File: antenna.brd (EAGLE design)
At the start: 95 x 95 mm, 21 parts, among them X1 BU-SMA-V

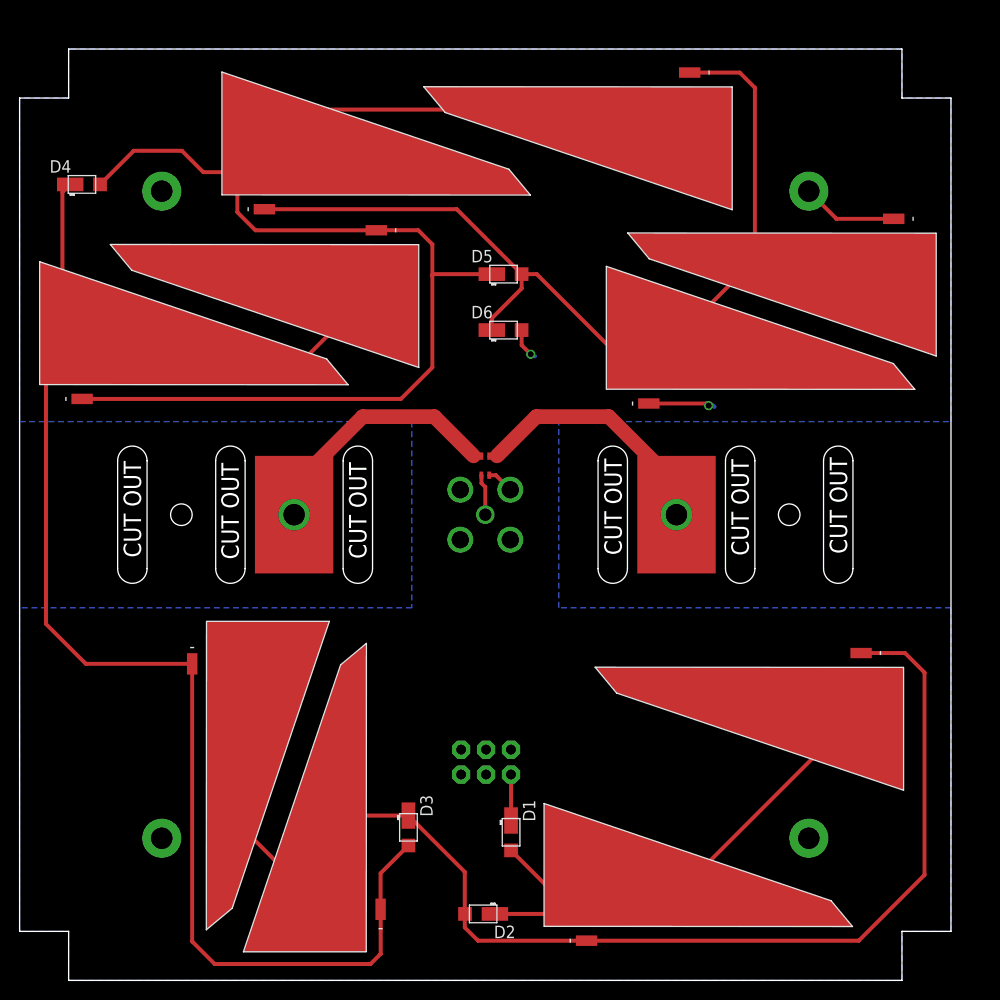
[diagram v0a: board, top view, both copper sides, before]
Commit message: Updates to antenna board
Fixed corner cutout dimensions. Added 3-pin Molex connector. Added
“CUTOUT” text to dimension layer.
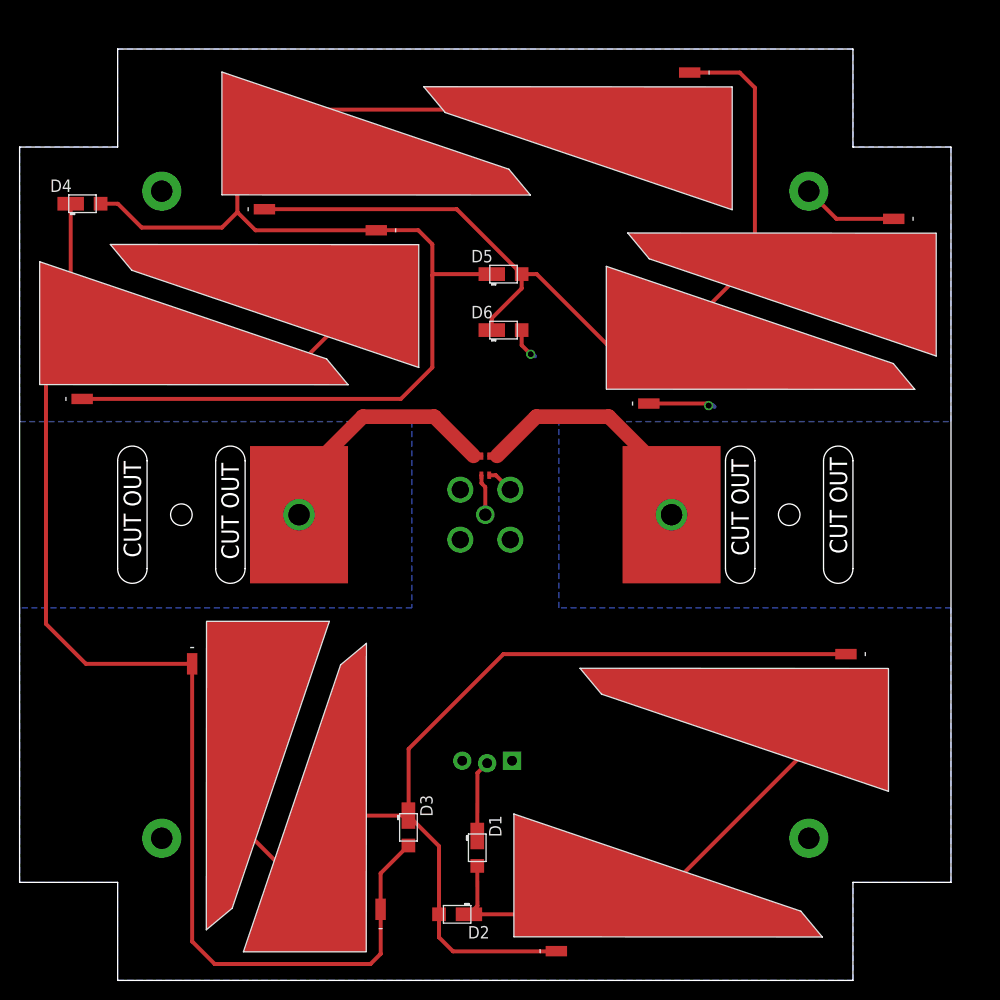
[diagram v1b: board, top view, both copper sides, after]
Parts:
- JP1: device SparkFun-Connectors:2X3 -> SparkFun-Connectors:MOLEX-1X3_LOCK
- moved D1 3.79 mm to (46.7, 13.5)
- moved SL1 3.26 mm to (57.8, 4.57)
- moved D2 2.65 mm to (44.6, 6.74)
- moved D4 1.97 mm to (6.41, 79.2)
- moved SL2 1.54 mm to (81.3, 31.7)
- moved JP1 1.28 mm to (50.2, 22.3)
- moved U$1 0.50 mm to (28.5, 47.5)
- moved U$2 0.50 mm to (66.5, 47.5)
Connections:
- net GND: now also JP1.1; no longer JP1.2
- net V_SOLAR: now also JP1.2; no longer JP1.1
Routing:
- net N$45: track 140.8 -> 130.7 mm
- net V_SOLAR: track 4.69 -> 7.83 mm
- net N$37: track 161.6 -> 160.2 mm
- net N$9: track 56.8 -> 57.7 mm
- net N$39: track 148.2 -> 147.6 mm
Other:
- outline, holes or cut-outs redrawn

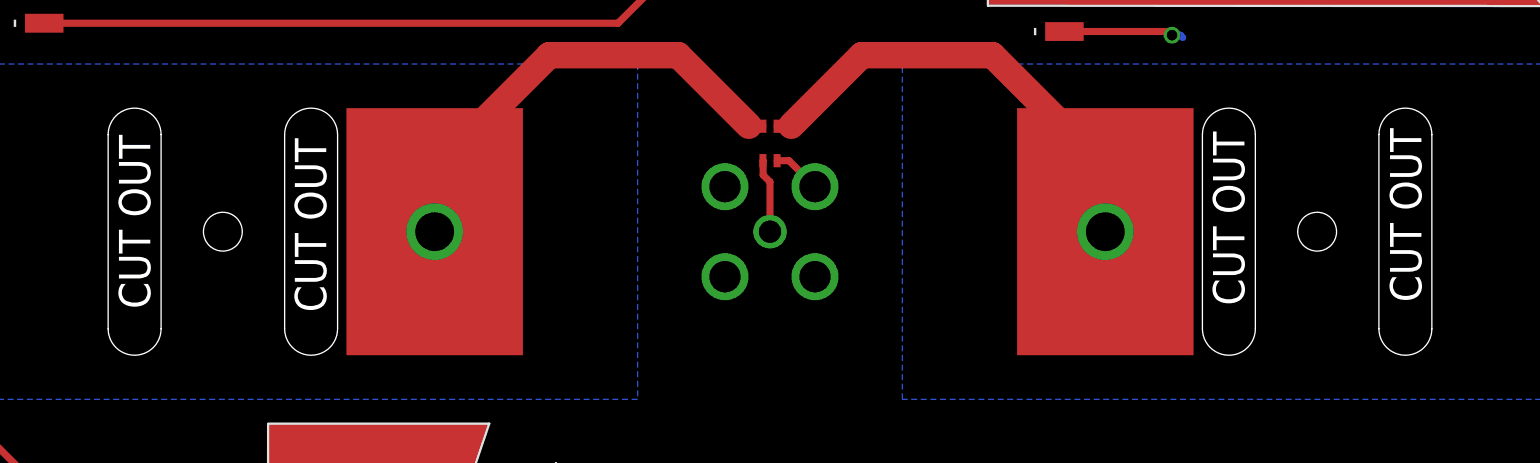
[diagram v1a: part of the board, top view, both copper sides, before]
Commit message: Increased cutout line width
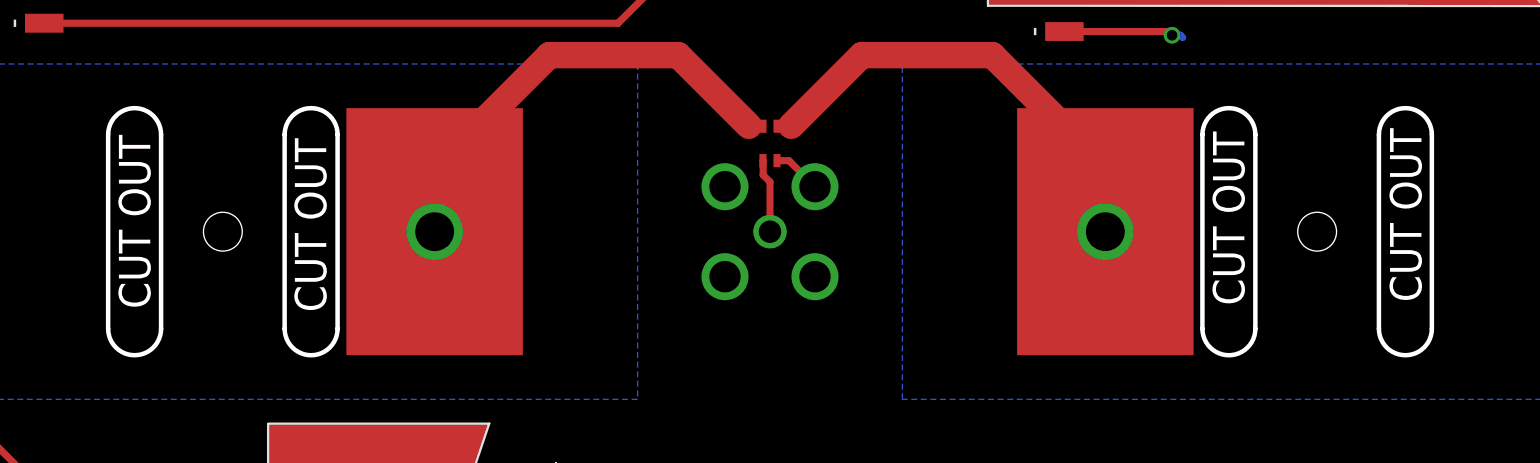
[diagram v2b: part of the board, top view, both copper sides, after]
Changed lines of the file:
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@@
 <wire x1="10" y1="85" x2="0" y2="85" width="0" layer="20"/>
 <wire x1="0" y1="85" x2="0" y2="10" width="0" layer="20"/>
-<wire x1="75" y1="53" x2="75" y2="42" width="0" layer="20"/>
-<wire x1="72" y1="42" x2="72" y2="53" width="0" layer="20"/>
-<wire x1="10" y1="42" x2="10" y2="53" width="0" layer="20"/>
-<wire x1="13" y1="53" x2="13" y2="42" width="0" layer="20"/>
-<wire x1="20" y1="42" x2="20" y2="53" width="0" layer="20"/>
-<wire x1="23" y1="53" x2="23" y2="42" width="0" layer="20"/>
-<wire x1="10" y1="53" x2="13" y2="53" width="0" layer="20" curve="-180" cap="flat"/>
-<wire x1="13" y1="42" x2="10" y2="42" width="0" layer="20" curve="-180" cap="flat"/>
-<wire x1="20" y1="53" x2="23" y2="53" width="0" layer="20" curve="-180" cap="flat"/>
-<wire x1="23" y1="42" x2="20" y2="42" width="0" layer="20" curve="-180" cap="flat"/>
-<wire x1="72" y1="53" x2="75" y2="53" width="0" layer="20" curve="-180" cap="flat"/>
-<wire x1="75" y1="42" x2="72" y2="42" width="0" layer="20" curve="-180" cap="flat"/>
-<wire x1="85" y1="53" x2="85" y2="42" width="0" layer="20"/>
-<wire x1="82" y1="42" x2="82" y2="53" width="0" layer="20"/>
-<wire x1="82" y1="53" x2="85" y2="53" width="0" layer="20" curve="-180" cap="flat"/>
-<wire x1="85" y1="42" x2="82" y2="42" width="0" layer="20" curve="-180" cap="flat"/>
+<wire x1="75" y1="53" x2="75" y2="42" width="0.254" layer="20"/>
+<wire x1="72" y1="42" x2="72" y2="53" width="0.254" layer="20"/>
+<wire x1="10" y1="42" x2="10" y2="53" width="0.254" layer="20"/>
+<wire x1="13" y1="53" x2="13" y2="42" width="0.254" layer="20"/>
+<wire x1="20" y1="42" x2="20" y2="53" width="0.254" layer="20"/>
+<wire x1="23" y1="53" x2="23" y2="42" width="0.254" layer="20"/>
+<wire x1="10" y1="53" x2="13" y2="53" width="0.254" layer="20" curve="-180" cap="flat"/>
+<wire x1="13" y1="42" x2="10" y2="42" width="0.254" layer="20" curve="-180" cap="flat"/>
+<wire x1="20" y1="53" x2="23" y2="53" width="0.254" layer="20" curve="-180" cap="flat"/>
+<wire x1="23" y1="42" x2="20" y2="42" width="0.254" layer="20" curve="-180" cap="flat"/>
+<wire x1="72" y1="53" x2="75" y2="53" width="0.254" layer="20" curve="-180" cap="flat"/>
+<wire x1="75" y1="42" x2="72" y2="42" width="0.254" layer="20" curve="-180" cap="flat"/>
+<wire x1="85" y1="53" x2="85" y2="42" width="0.254" layer="20"/>
+<wire x1="82" y1="42" x2="82" y2="53" width="0.254" layer="20"/>
+<wire x1="82" y1="53" x2="85" y2="53" width="0.254" layer="20" curve="-180" cap="flat"/>
+<wire x1="85" y1="42" x2="82" y2="42" width="0.254" layer="20" curve="-180" cap="flat"/>
 <circle x="47.5" y="47.7" radius="7.25" width="0.4" layer="22"/>
 <hole x="16.5" y="47.5" drill="2.2"/>

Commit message: Cleanup
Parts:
- added FRAME1: FRAME-LETTER, SparkFun-Aesthetics:CREATIVE_COMMONS
- added U$3: KICKSAT_LOGO, KickSat-Logo:KICKSAT_LOGO
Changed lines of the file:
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@@
 <element name="SL10" library="phonesat" package="SOLAR_CELL" value="SOLAR_CELL" x="67.18" y="60.43" rot="R90"/>
 <element name="JP1" library="SparkFun-Connectors" package="MOLEX-1X3_LOCK" value="" x="50.23" y="22.28" rot="MR0"/>
+<element name="FRAME1" library="SparkFun-Aesthetics" package="CREATIVE_COMMONS" value="FRAME-LETTER" x="20.71" y="-7.66"/>
+<element name="U$3" library="KickSat-Logo" package="KICKSAT_LOGO" value="KICKSAT_LOGO" x="59.98" y="25.85" rot="MR0"/>
 </elements>
 <signals>

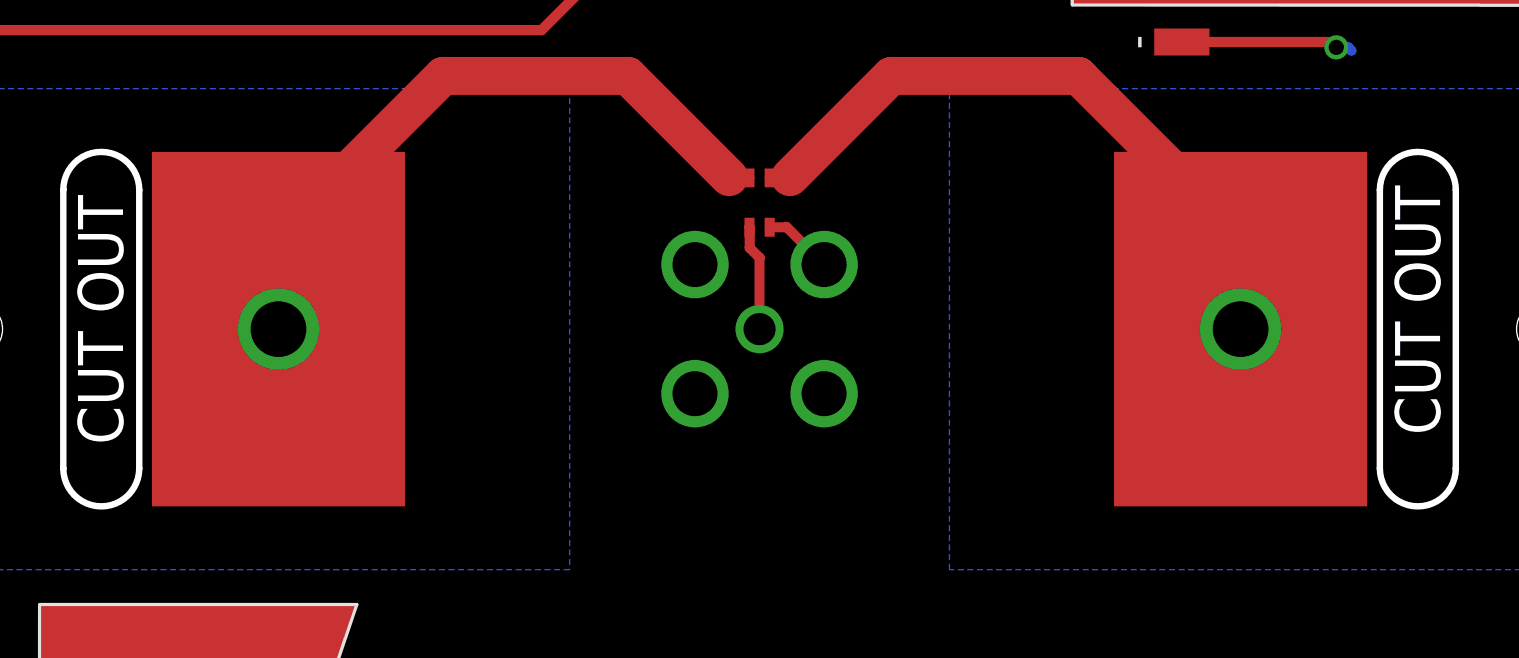
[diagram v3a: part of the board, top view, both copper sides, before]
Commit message: Fixed solar cell footprints
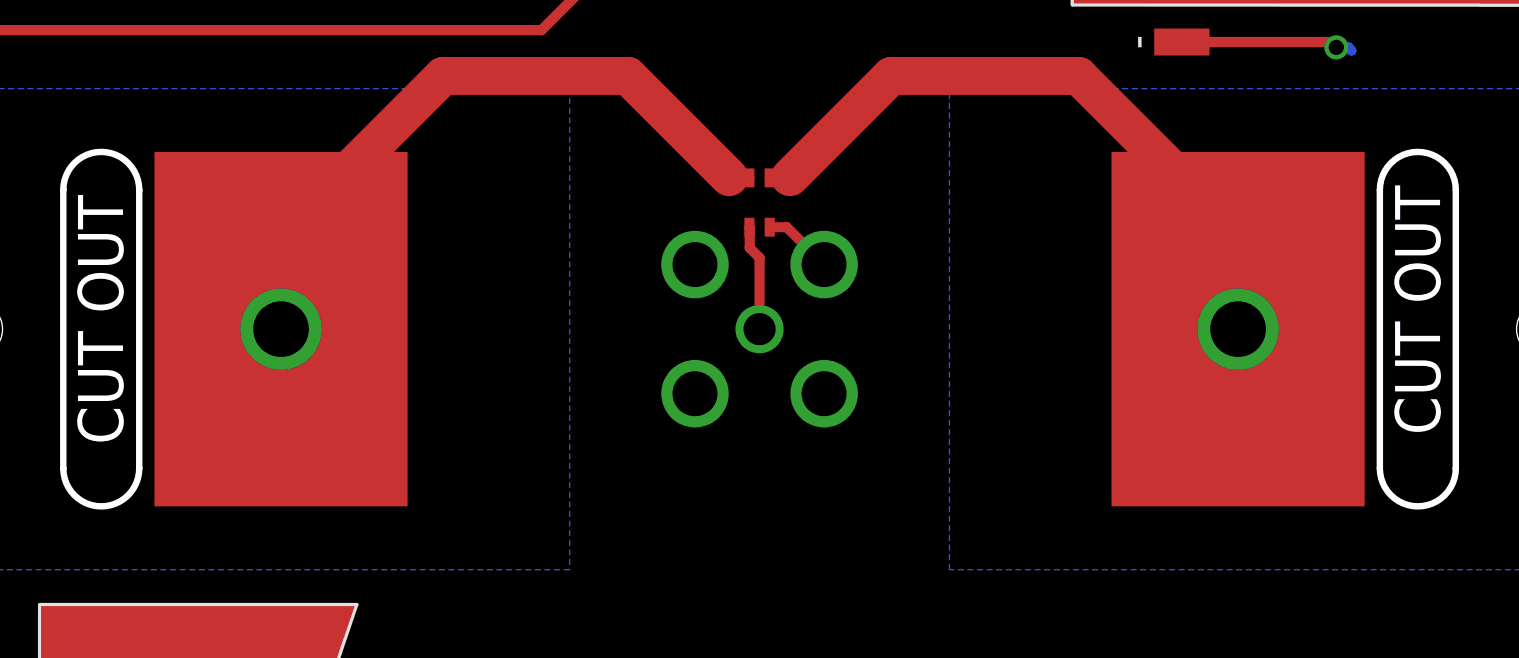
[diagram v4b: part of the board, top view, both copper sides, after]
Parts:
- D1, D2, D3, D4, D5, D6: device phonesat:SB_DIODE -> Solar:SB_DIODE
- SL1, SL10, SL2, SL3, SL4, SL5, SL6, SL7, SL8, SL9: device phonesat:SOLAR_CELL -> Solar:SOLAR_CELL
- moved U$1 0.10 mm to (28.6, 47.5)
- moved U$2 0.10 mm to (66.4, 47.5)
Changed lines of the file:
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@@
 </element>
 <element name="B1" library="Balun" package="BALUN" value="BALUN" x="47.5" y="52.5" smashed="yes" rot="R90"/>
-<element name="U$1" library="TapeAntenna" package="TAPEANTENNA" value="TAPEANTENNA" x="28.5" y="47.5"/>
-<element name="U$2" library="TapeAntenna" package="TAPEANTENNA" value="TAPEANTENNA" x="66.5" y="47.5"/>
-<element name="SL3" library="phonesat" package="SOLAR_CELL" value="SOLAR_CELL" x="35.23" y="10.25" rot="R180"/>
-<element name="D3" library="phonesat" package="SB_DIODE" value="SB_DIODE" x="39.66" y="15.61" rot="R270"/>
-<element name="SL4" library="phonesat" package="SOLAR_CELL" value="SOLAR_CELL" x="19.19" y="29.29"/>
-<element name="SL1" library="phonesat" package="SOLAR_CELL" value="SOLAR_CELL" x="57.75" y="4.57" rot="R90"/>
-<element name="SL7" library="phonesat" package="SOLAR_CELL" value="SOLAR_CELL" x="65.35" y="91.01" rot="R270"/>
-<element name="SL8" library="phonesat" package="SOLAR_CELL" value="SOLAR_CELL" x="27.97" y="80.25" rot="R90"/>
-<element name="SL2" library="phonesat" package="SOLAR_CELL" value="SOLAR_CELL" x="81.29" y="31.69" rot="R270"/>
-<element name="D2" library="phonesat" package="SB_DIODE" value="SB_DIODE" x="44.63" y="6.74" rot="R180"/>
-<element name="D4" library="phonesat" package="SB_DIODE" value="SB_DIODE" x="6.41" y="79.22"/>
-<element name="D5" library="phonesat" package="SB_DIODE" value="SB_DIODE" x="49.36" y="72.04"/>
-<element name="D6" library="phonesat" package="SB_DIODE" value="SB_DIODE" x="49.36" y="66.33"/>
-<element name="D1" library="phonesat" package="SB_DIODE" value="SB_DIODE" x="46.68" y="13.53" rot="R270"/>
-<element name="SL6" library="phonesat" package="SOLAR_CELL" value="SOLAR_CELL" x="9.38" y="60.9" rot="R90"/>
-<element name="SL5" library="phonesat" package="SOLAR_CELL" value="SOLAR_CELL" x="33.38" y="74.92" rot="R270"/>
-<element name="SL9" library="phonesat" package="SOLAR_CELL" value="SOLAR_CELL" x="86.16" y="76.09" rot="R270"/>
-<element name="SL10" library="phonesat" package="SOLAR_CELL" value="SOLAR_CELL" x="67.18" y="60.43" rot="R90"/>
+<element name="U$1" library="TapeAntenna" package="TAPEANTENNA" value="TAPEANTENNA" x="28.6" y="47.5"/>
+<element name="U$2" library="TapeAntenna" package="TAPEANTENNA" value="TAPEANTENNA" x="66.4" y="47.5"/>
+<element name="SL3" library="Solar" package="SOLAR_CELL" value="SOLAR_CELL" x="35.23" y="10.25" rot="R180"/>
+<element name="D3" library="Solar" package="SB_DIODE" value="SB_DIODE" x="39.66" y="15.61" rot="R270"/>
+<element name="SL4" library="Solar" package="SOLAR_CELL" value="SOLAR_CELL" x="19.19" y="29.29"/>
+<element name="SL1" library="Solar" package="SOLAR_CELL" value="SOLAR_CELL" x="57.75" y="4.57" rot="R90"/>
+<element name="SL7" library="Solar" package="SOLAR_CELL" value="SOLAR_CELL" x="65.35" y="91.01" rot="R270"/>
+<element name="SL8" library="Solar" package="SOLAR_CELL" value="SOLAR_CELL" x="27.97" y="80.25" rot="R90"/>
+<element name="SL2" library="Solar" package="SOLAR_CELL" value="SOLAR_CELL" x="81.29" y="31.69" rot="R270"/>
+<element name="D2" library="Solar" package="SB_DIODE" value="SB_DIODE" x="44.63" y="6.74" rot="R180"/>
+<element name="D4" library="Solar" package="SB_DIODE" value="SB_DIODE" x="6.41" y="79.22"/>
+<element name="D5" library="Solar" package="SB_DIODE" value="SB_DIODE" x="49.36" y="72.04"/>
+<element name="D6" library="Solar" package="SB_DIODE" value="SB_DIODE" x="49.36" y="66.33"/>
+<element name="D1" library="Solar" package="SB_DIODE" value="SB_DIODE" x="46.68" y="13.53" rot="R270"/>
+<element name="SL6" library="Solar" package="SOLAR_CELL" value="SOLAR_CELL" x="9.38" y="60.9" rot="R90"/>
+<element name="SL5" library="Solar" package="SOLAR_CELL" value="SOLAR_CELL" x="33.38" y="74.92" rot="R270"/>
+<element name="SL9" library="Solar" package="SOLAR_CELL" value="SOLAR_CELL" x="86.16" y="76.09" rot="R270"/>
+<element name="SL10" library="Solar" package="SOLAR_CELL" value="SOLAR_CELL" x="67.18" y="60.43" rot="R90"/>
 <element name="JP1" library="SparkFun-Connectors" package="MOLEX-1X3_LOCK" value="" x="50.23" y="22.28" rot="MR0"/>
 <element name="FRAME1" library="SparkFun-Aesthetics" package="CREATIVE_COMMONS" value="FRAME-LETTER" x="20.71" y="-7.66"/>
@@
 <via x="14.5" y="14.5" extent="1-16" drill="2.2" diameter="4"/>
 <via x="80.5" y="14.5" extent="1-16" drill="2.2" diameter="4"/>
-<polygon width="0.4064" layer="16">
+<polygon width="1" layer="16">
 <vertex x="0" y="57"/>
 <vertex x="40" y="57"/>
@@
 <wire x1="35" y1="57.5" x2="42.3" y2="57.5" width="1.5" layer="1"/>
 <wire x1="42.3" y1="57.5" x2="46.3" y2="53.5" width="1.5" layer="1"/>
-<wire x1="28.5" y1="47.5" x2="28.5" y2="51" width="1.5" layer="1"/>
+<wire x1="28.6" y1="47.5" x2="28.5" y2="51" width="1.5" layer="1"/>
 <wire x1="28.5" y1="51" x2="35" y2="57.5" width="1.5" layer="1"/>
 </signal>
@@
 <wire x1="60.1" y1="57.5" x2="52.7" y2="57.5" width="1.5" layer="1"/>
 <wire x1="52.7" y1="57.5" x2="48.7" y2="53.5" width="1.5" layer="1"/>
-<wire x1="66.5" y1="47.5" x2="66.5" y2="51.1" width="1.5" layer="1"/>
+<wire x1="66.4" y1="47.5" x2="66.5" y2="51.1" width="1.5" layer="1"/>
 <wire x1="66.5" y1="51.1" x2="60.1" y2="57.5" width="1.5" layer="1"/>
 </signal>
